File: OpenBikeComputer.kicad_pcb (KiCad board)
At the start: 4 copper layers, 80 x 80 mm, 53 parts, among them J1 USB_C_Receptacle_USB2.0_14P, J2 RJ45_Shielded, J4 Micro_SD_Card_Det1, J5 Conn_01x24_Socket, J6 Conn_01x03_Pin, J7 RFShield_TwoPieces, J8 Conn_01x02_Socket, U1 nRF54L15-QFXX, U2 nPM1300-QEXX, U3 BQ298012RUGR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

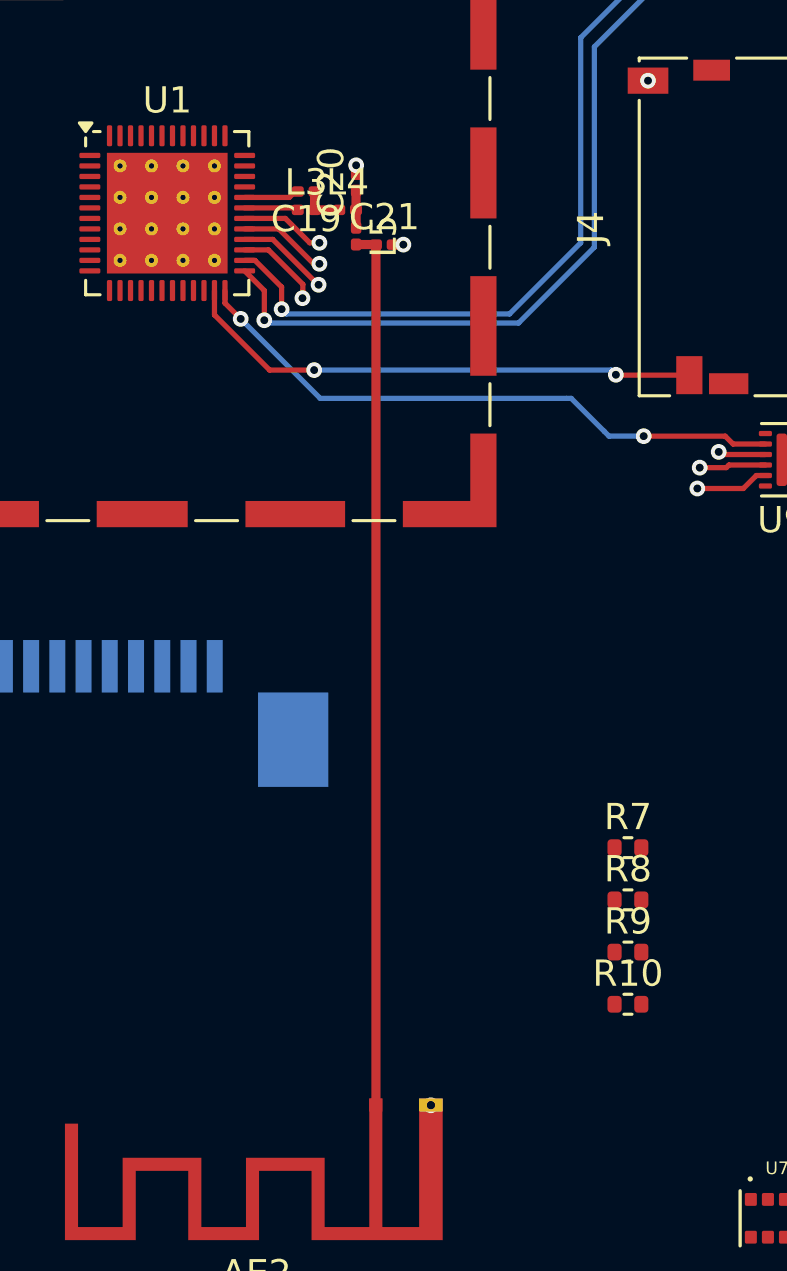
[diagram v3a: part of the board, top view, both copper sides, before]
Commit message: fixup antenna trace stuff
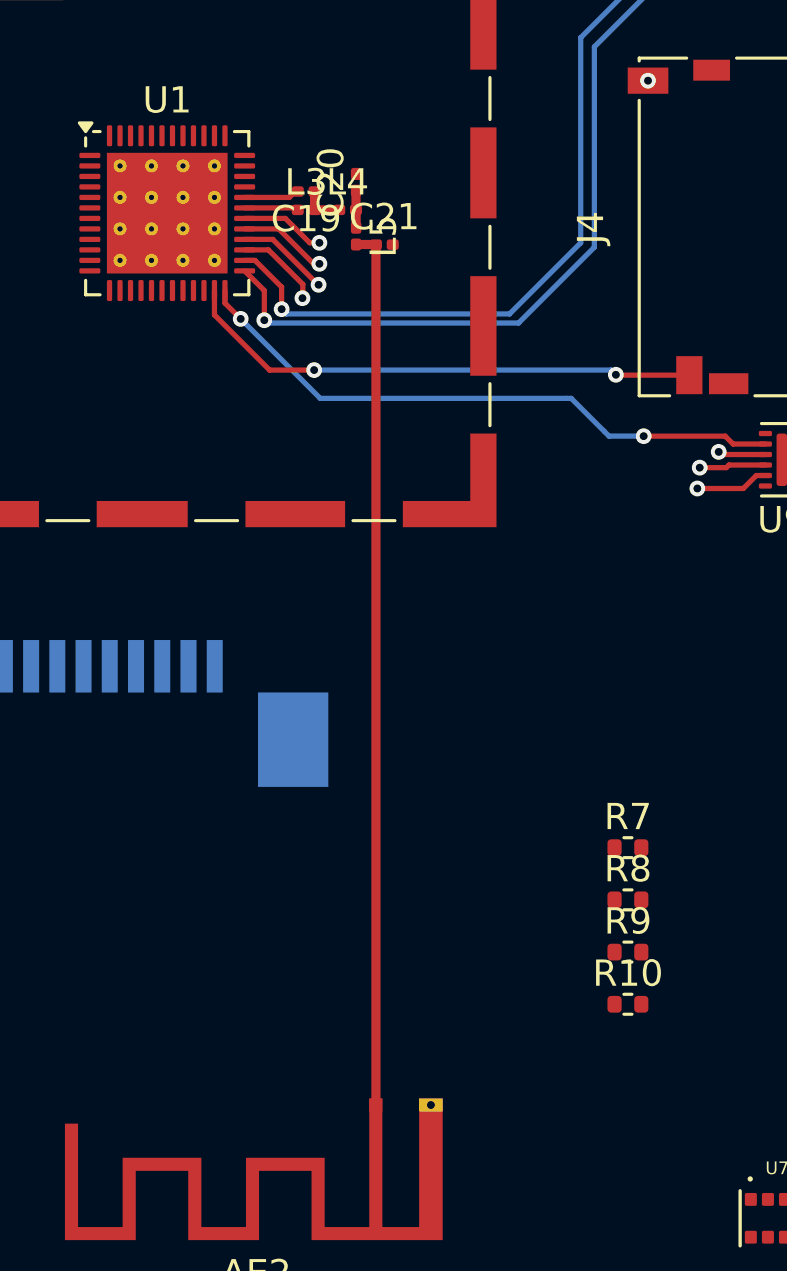
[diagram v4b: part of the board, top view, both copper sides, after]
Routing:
- net GND: track 7.81 -> 7.00 mm, vias 15 -> 12
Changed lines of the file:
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@@
 			(net 75 "GND")
 			(pintype "passive")
+			(zone_connect 2)
+			(teardrops
+				(best_length_ratio 0.5)
+				(max_length 1)
+				(best_width_ratio 1)
+				(max_width 2)
+				(curve_points 0)
+				(filter_ratio 0.9)
+				(enabled no)
+				(allow_two_segments yes)
+				(prefer_zone_connections no)
+			)
 		)
 		(model "${KICAD8_3DMODEL_DIR}/Capacitor_SMD.3dshapes/C_0201_0603Metric.wrl"
@@
 			(net 75 "GND")
 			(pintype "passive")
+			(zone_connect 2)
 		)
 		(model "${KICAD8_3DMODEL_DIR}/Capacitor_SMD.3dshapes/C_0201_0603Metric.wrl"
@@
 			(net 75 "GND")
 			(pintype "passive")
+			(zone_connect 2)
 		)
 		(model "${KICAD8_3DMODEL_DIR}/Capacitor_SMD.3dshapes/C_0201_0603Metric.wrl"
@@
 	)
 	(segment
-		(start 207.099901 112.654873)
-		(end 207.099901 112.324873)
-		(width 0.35)
-		(layer "F.Cu")
-		(net 75)
-	)
-	(segment
 		(start 204.551261 113.550127)
 		(end 204.776515 113.324873)
@@
 	)
 	(segment
-		(start 208.494901 115.349873)
-		(end 208.899901 115.349873)
-		(width 0.35)
-		(layer "F.Cu")
-		(net 75)
-	)
-	(segment
 		(start 192.125735 86.724265)
 		(end 192.125735 86.674265)
@@
 	)
 	(segment
-		(start 207.124901 112.654873)
-		(end 207.124901 112.57434)
-		(width 0.2)
-		(layer "F.Cu")
-		(net 75)
-	)
-	(segment
 		(start 218.774746 93.575254)
 		(end 218.775 93.575)
@@
 	)
 	(via
-		(at 208.899901 115.349873)
-		(size 0.6)
-		(drill 0.3)
-		(layers "F.Cu" "B.Cu")
-		(net 75)
-	)
-	(via
 		(at 192.125735 86.724265)
 		(size 0.6)
@@
 	)
 	(via
-		(at 207.099901 112.324873)
-		(size 0.6)
-		(drill 0.3)
-		(layers "F.Cu" "B.Cu")
-		(net 75)
-	)
-	(via
 		(at 194.95 82.255)
 		(size 0.6)
@@
 	)
 	(via
-		(at 209.94993 148.155)
-		(size 0.6)
-		(drill 0.3)
-		(layers "F.Cu" "B.Cu")
-		(net 75)
-	)
-	(via
 		(at 208.25 87.25)
 		(size 0.6)
@@
 	)
 	(zone
+		(net 75)
+		(net_name "GND")
+		(layer "F.Cu")
+		(name "$teardrop_padvia$")
+		(hatch full 0.1)
+		(priority 30000)
+		(attr
+			(teardrop
+				(type padvia)
+			)
+		)
+		(connect_pads yes
+			(clearance 0)
+		)
+		(min_thickness 0.0254)
+		(filled_areas_thickness no)
+		(fill yes
+			(thermal_gap 0.5)
+			(thermal_bridge_width 0.5)
+			(island_removal_mode 1)
+			(island_area_min 10)
+		)
+		(polygon
+			(pts
+				(xy 192.661447 86.421396) (xy 192.378604 86.138553) (xy 191.913603 86.512133) (xy 192.125028 86.724972)
+				(xy 192.402899 86.83907)
+			)
+		)
+	)
+	(zone
 		(net 0)
 		(net_name "")
@@
 	)
 	(zone
-		(net 75)
-		(net_name "GND")
-		(layer "F.Cu")
-		(name "$teardrop_padvia$")
-		(hatch full 0.1)
-		(priority 30000)
-		(attr
-			(teardrop
-				(type padvia)
-			)
-		)
-		(connect_pads yes
-			(clearance 0)
-		)
-		(min_thickness 0.0254)
-		(filled_areas_thickness no)
-		(fill yes
-			(thermal_gap 0.5)
-			(thermal_bridge_width 0.5)
-			(island_removal_mode 1)
-			(island_area_min 10)
-		)
-		(polygon
-			(pts
-				(xy 192.661447 86.421396) (xy 192.378604 86.138553) (xy 191.913603 86.512133) (xy 192.125028 86.724972)
-				(xy 192.402899 86.83907)
-			)
-		)
-	)
-	(zone
 		(net 0)
 		(net_name "")
@@
 		(polygon
 			(pts
-				(xy 192.5 155) (xy 214 155.025) (xy 214 147.5) (xy 206.25 147.5) (xy 206.25 144) (xy 192.5 144)
+				(xy 192.5 155) (xy 214 155.025) (xy 214.025 148.4) (xy 209.25 148.4) (xy 209.25 147.5) (xy 206.25 147.5)
+				(xy 206.25 144) (xy 192.5 144)
 			)
 		)

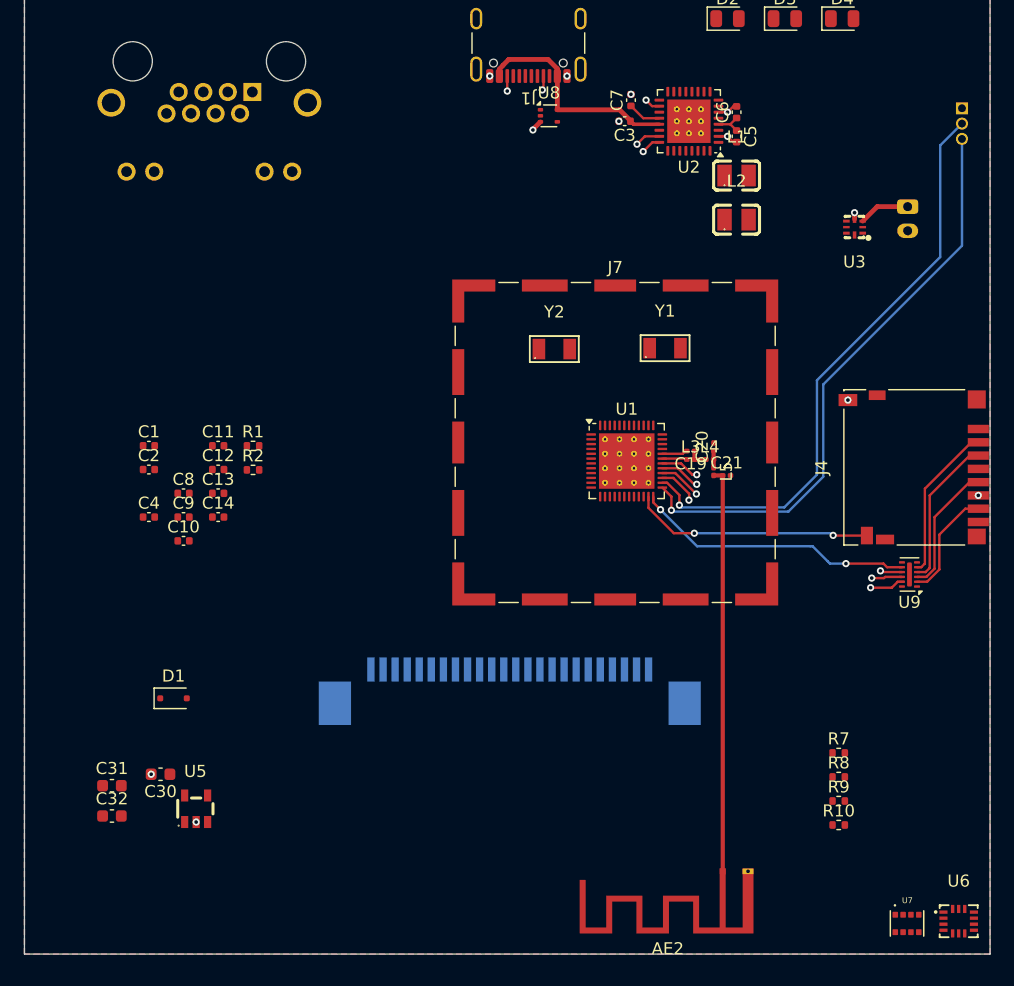
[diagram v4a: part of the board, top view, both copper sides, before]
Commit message: clarify and set up board stackup properly
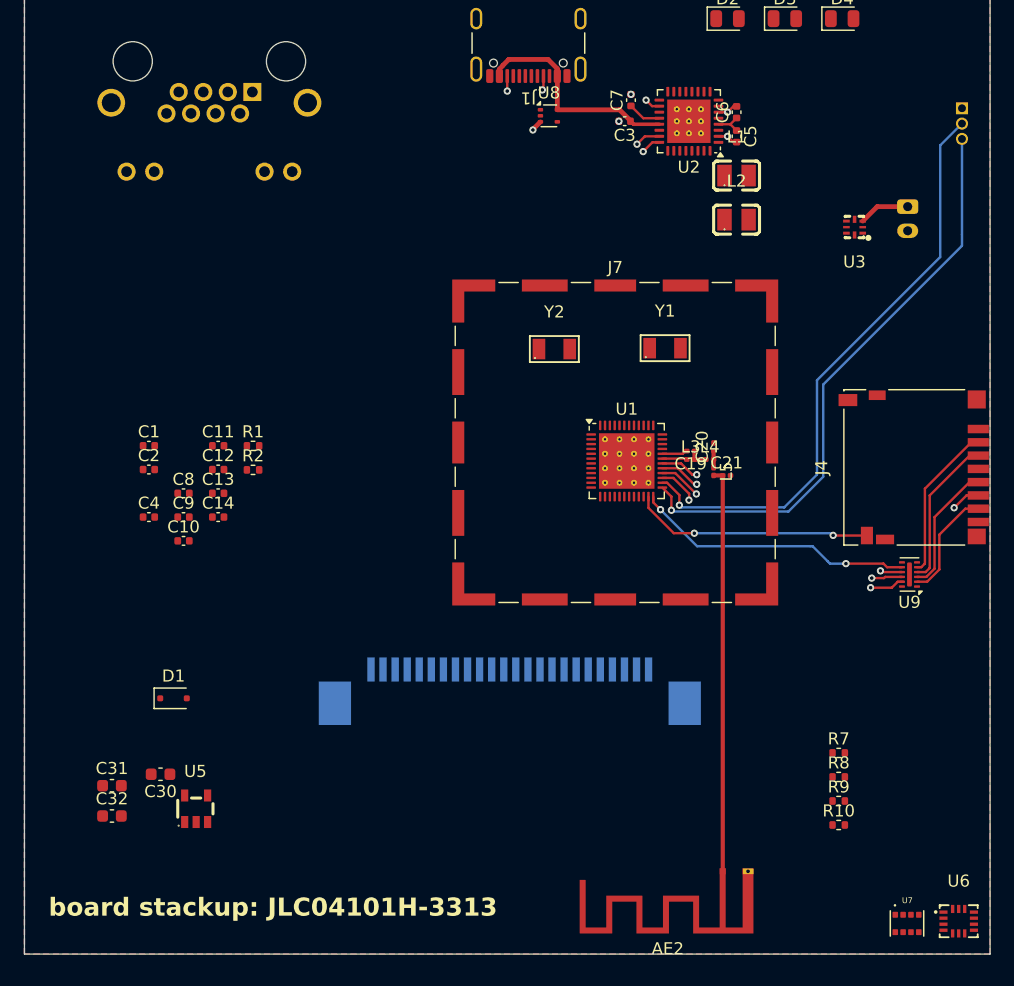
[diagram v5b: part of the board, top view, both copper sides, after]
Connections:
- U1 pad 30: unconnected-(U1-~{RESET}-Pad30) -> VDDIO
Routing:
- net unconnected-(U1-~{RESET}-Pad30): track 3.24 -> 0.00 mm, vias 1 -> 0
- net VDDIO: track 0.00 -> 3.24 mm, vias 0 -> 1
- net GND: track 7.00 -> 8.87 mm, vias 12 -> 6
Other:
- board text added: "board stackup: JLC04101H-3313"

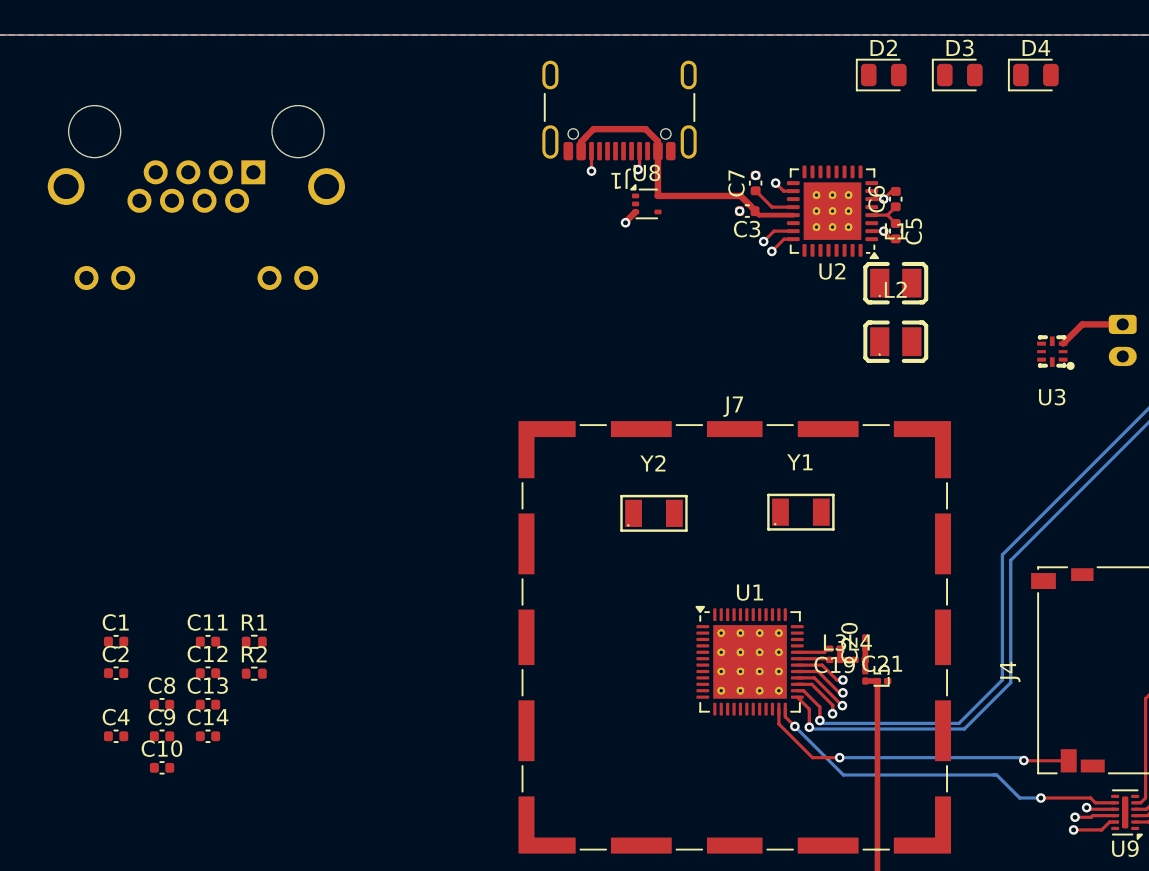
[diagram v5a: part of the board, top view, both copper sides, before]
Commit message: rfinish routing PMIC (pretty crap routing)
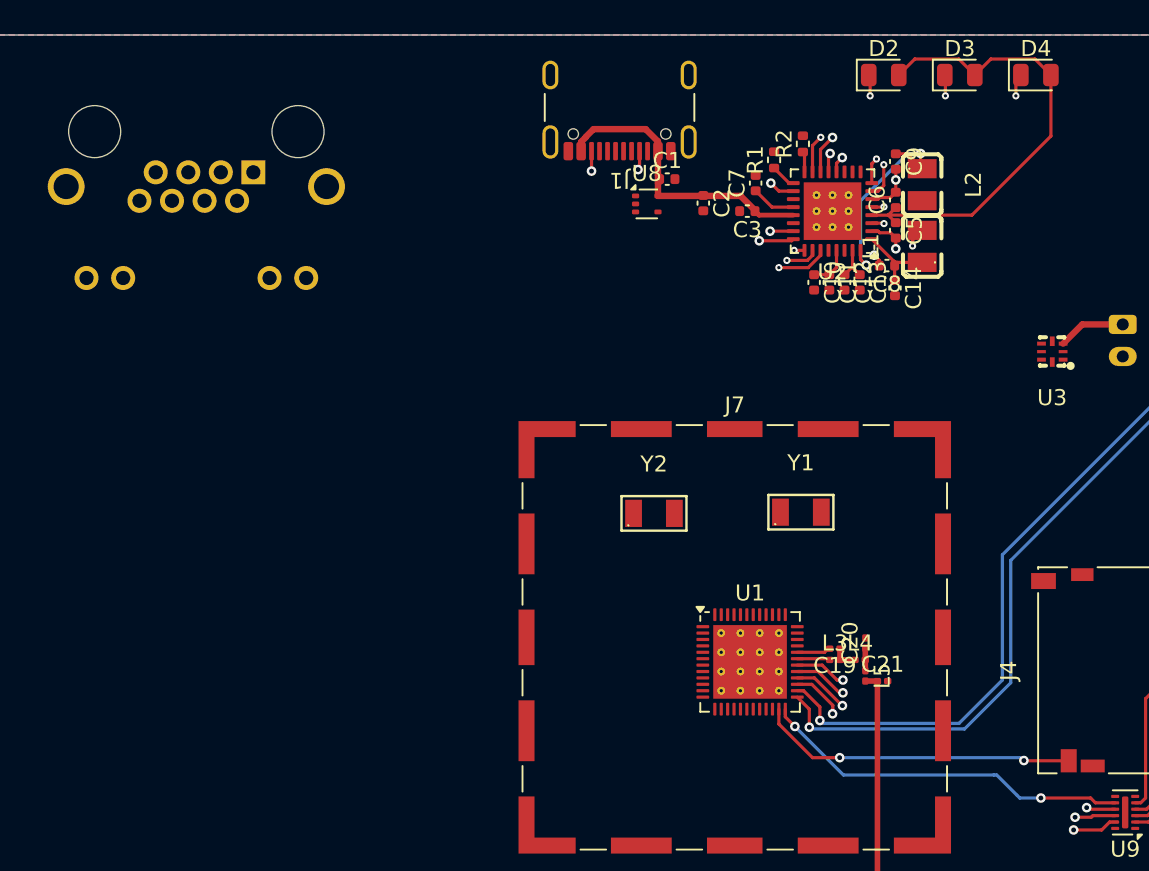
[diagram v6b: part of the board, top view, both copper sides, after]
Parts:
- removed C4: 1.0uF, Capacitor_SMD:C_0402_1005Metric
- moved C9 58.2 mm to (209.0, 82.9), turned to -90 degrees
- moved C8 52.9 mm to (208.4, 89.4), turned to 180 degrees
- moved C14 51.2 mm to (208.9, 90.8), turned to -90 degrees
- moved C10 50.8 mm to (203.9, 90.5), turned to -90 degrees
- moved C13 48.5 mm to (206.8, 90.5), turned to -90 degrees
- moved R2 47.6 mm to (203.2, 81.8), turned to 90 degrees
- moved C2 47.0 mm to (197.0, 85.5), turned to -90 degrees
- moved C12 46.6 mm to (205.8, 90.5), turned to -90 degrees
- moved C1 44.9 mm to (194.7, 84.0)
- moved C11 44.8 mm to (204.8, 90.5), turned to -90 degrees
- moved R1 44.3 mm to (201.4, 82.8), turned to 90 degrees
- moved L2 9.94 mm to (210.7, 84.3), turned to -90 degrees
- moved L1 2.83 mm to (210.7, 88.2), turned to 90 degrees
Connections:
- U2 pad 22: /Power/VUSBOUT -> Net-(U2-VBUSOUT)
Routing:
- net VSYS: track 5.22 -> 32.3 mm
- net Net-(D4-K): track 0.00 -> 23.5 mm, vias 0 -> 2
- net Net-(D3-K): track 0.00 -> 21.4 mm, vias 0 -> 2
- net Net-(D2-K): track 0.00 -> 19.2 mm, vias 0 -> 2
- net /Display/3.0V: track 0.00 -> 13.2 mm, vias 0 -> 2
- net VDDIO: track 3.24 -> 9.25 mm, vias 1 -> 2
- net Net-(U2-SW1): track 0.00 -> 4.36 mm, vias 0 -> 2
- net VOUTLDO1: track 0.00 -> 2.66 mm
- net SCL1: track 0.00 -> 2.46 mm, vias 0 -> 1
- net VOUTLDO2: track 0.00 -> 2.41 mm
- net Net-(U2-SHPHLD): track 0.00 -> 2.37 mm, vias 0 -> 1
- net /MCU/RESET: track 0.00 -> 2.19 mm, vias 0 -> 1
- net GND: track 8.87 -> 10.8 mm, vias 6 -> 4
- net /MCU/INT: track 0.00 -> 1.63 mm, vias 0 -> 1
- net Net-(U2-VSET1): track 0.00 -> 1.59 mm
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
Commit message: shitty routing job for rev1
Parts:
- removed C10, C11, C12, C13: 10uF, Capacitor_SMD:C_0402_1005Metric
- added C22: 10uF, Capacitor_SMD:C_0201_0603Metric, F.Cu at (201.3, 118.8)
- added C23: 100nF, Capacitor_SMD:C_0201_0603Metric, F.Cu at (197.4, 109.8)
- added C24: 100nF, Capacitor_SMD:C_0201_0603Metric, F.Cu at (204.2, 111.0)
- added C25: 100nF, Capacitor_SMD:C_0201_0603Metric, F.Cu at (198.1, 109.8)
- added C26: 100nF, Capacitor_SMD:C_0201_0603Metric, F.Cu at (195.5, 115.6)
- R7, R8: moved to B.Cu
- moved R8 35.4 mm to (204.2, 107.5), turned to 180 degrees
- moved R7 34.8 mm to (203.5, 106.5), turned to 180 degrees
- moved Y1 6.81 mm to (205.9, 111.0), turned to 90 degrees
- moved Y2 5.87 mm to (194.9, 110.7), turned to -90 degrees
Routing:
- net VDDIO: track 9.25 -> 150.7 mm, vias 2 -> 9
- net SENSE2A: track 0.00 -> 54.9 mm, vias 0 -> 1
- net DETECT1: track 0.00 -> 52.8 mm, vias 0 -> 1
- net SENSE1A: track 0.00 -> 52.7 mm, vias 0 -> 1
- net SENSE2B: track 0.00 -> 49.3 mm, vias 0 -> 1
- net DETECT2: track 0.00 -> 48.6 mm, vias 0 -> 1
- net SENSE1B: track 0.00 -> 47.7 mm, vias 0 -> 1
- net SCL1: track 2.46 -> 33.1 mm, vias 1 -> 2
- net SDA1: track 1.19 -> 31.5 mm, vias 1 -> 2
- net /Display/MOSI: track 0.00 -> 21.2 mm, vias 0 -> 1
- net /Display/SCLK: track 0.00 -> 19.1 mm, vias 0 -> 1
- net Net-(U1-XC2): track 0.00 -> 4.48 mm
- net Net-(U1-P1.00): track 0.00 -> 3.40 mm
- net Net-(U1-XC1): track 0.00 -> 3.27 mm
- net /Display/DISPLAY_SHDN: track 0.00 -> 3.14 mm, vias 0 -> 1
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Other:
- board text added: "20250126_ly2_s6_w12"
